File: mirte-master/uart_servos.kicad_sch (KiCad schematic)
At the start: 2 parts, among them J5 servo_connector, J6 servo_connector_small

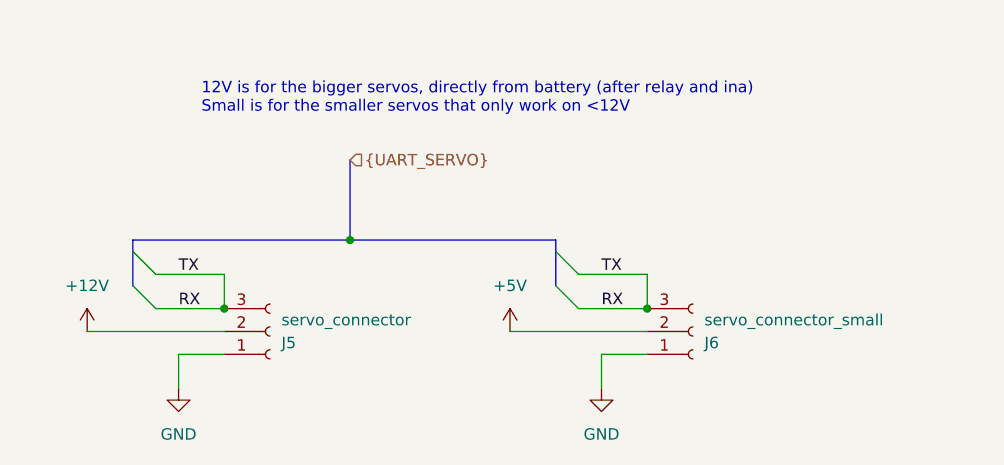
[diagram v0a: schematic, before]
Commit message: mirte-master schematic cleanup and readabilityimprovements
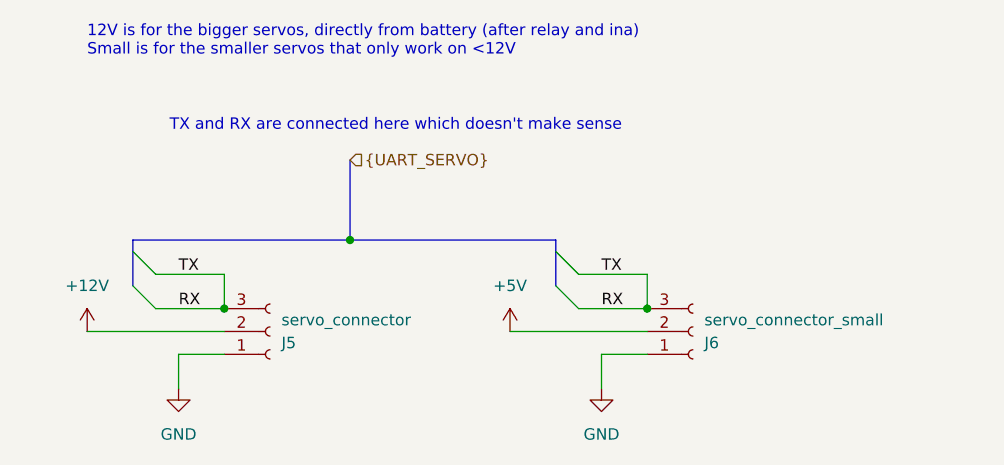
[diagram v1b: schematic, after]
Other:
- note added: "TX and RX are connected here which doesn't make sense"
- title: (none) -> ${PROJECTNAME}

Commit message: Change comment uart servos rx tx
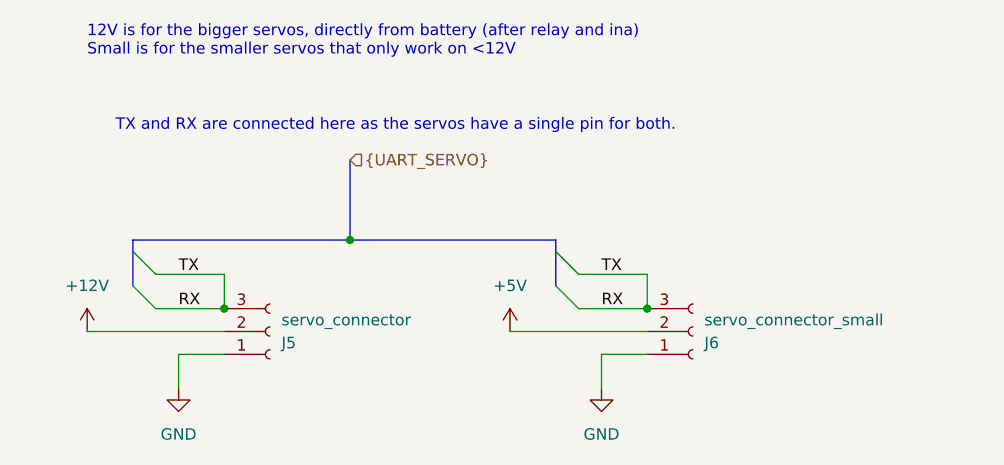
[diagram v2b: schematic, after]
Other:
- note added: "TX and RX are connected here as the servos have a single pin for both."
- note removed: "TX and RX are connected here which doesn't make sense"
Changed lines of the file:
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@@
 		)
 	)
-	(text "TX and RX are connected here which doesn't make sense"
+	(text "TX and RX are connected here as the servos have a single pin for both."
 		(exclude_from_sim no)
 		(at 135.89 66.04 0)
